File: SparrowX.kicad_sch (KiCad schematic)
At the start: 25 parts, among them J1 NORTH, J2 SOUTH, J3 WEST, J4 EAST, U1 TPS629210-Q1, U2 LD49100PU33RY, U3 STM32G0B1CBU6, U4 TCAN332G, U5 TCAN332G

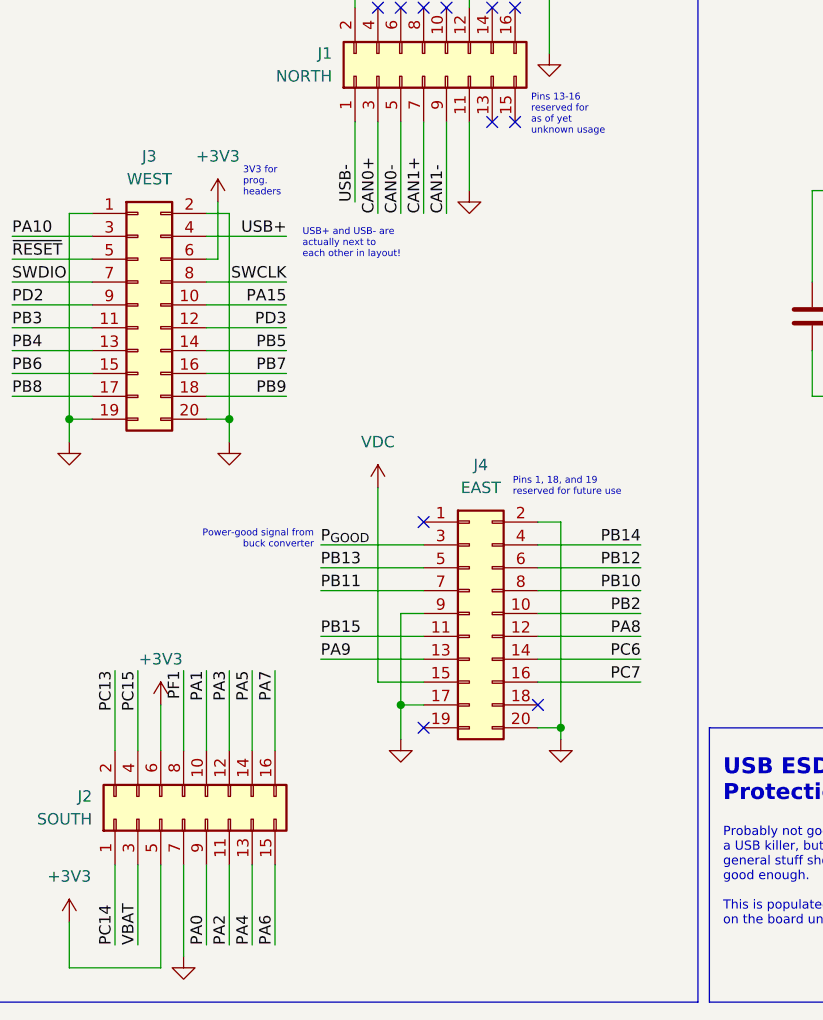
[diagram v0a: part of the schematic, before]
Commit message: Oops: fix missing PF0 pin
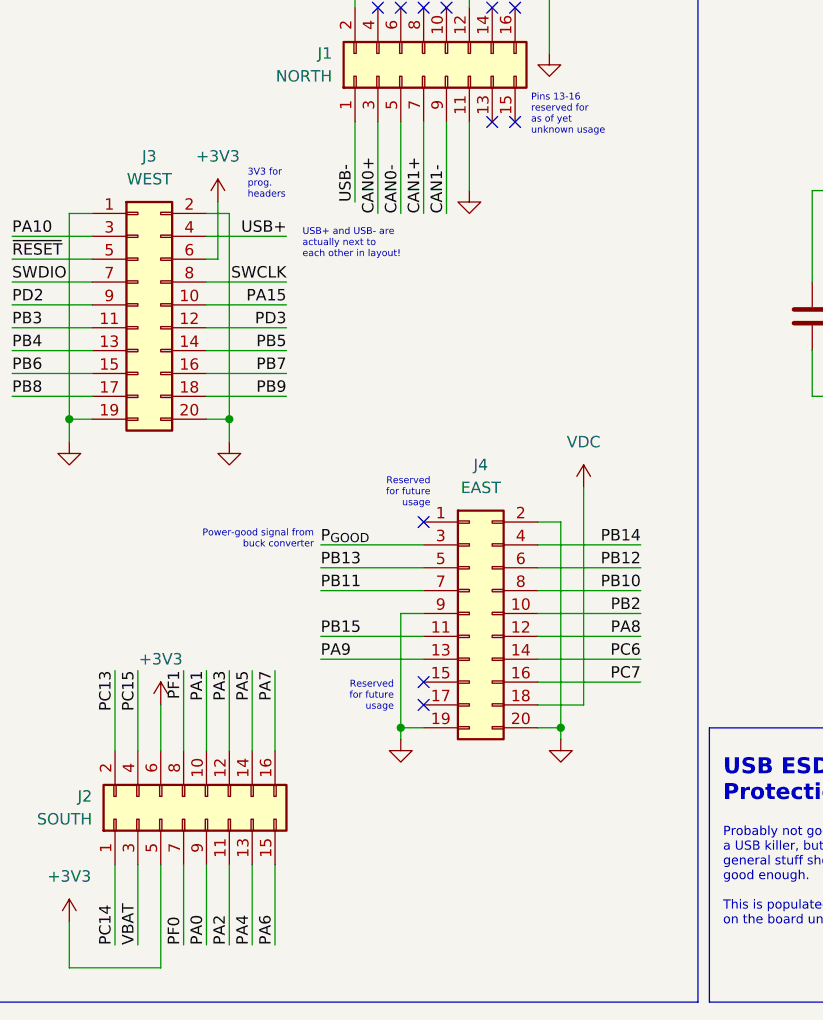
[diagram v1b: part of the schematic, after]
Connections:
- net GND: now also J4.19 (Pin_19); no longer J2.7 (Pin_7), J4.17 (Pin_17)
- net PF0: now also J2.7 (Pin_7)
- net VDC: now also J4.18 (Pin_18); no longer J4.15 (Pin_15)
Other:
- note added: "Reserved for future usage"
- note removed: "Pins 1, 18, and 19 reserved for future use"
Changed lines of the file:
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@@
 	)
 	(junction
-		(at 64.77 162.56)
-		(diameter 0)
-		(color 0 0 0 0)
-	)
-	(junction
 		(at 83.82 57.15)
 		(diameter 0)
@@
 	)
 	(junction
+		(at 64.77 165.1)
+		(diameter 0)
+		(color 0 0 0 0)
+	)
+	(junction
 		(at 30.48 33.02)
 		(diameter 0)
@@
 	)
 	(no_connect
-		(at 67.31 165.1)
-	)
-	(no_connect
-		(at 80.01 162.56)
+		(at 67.31 162.56)
 	)
 	(no_connect
@@
 	)
 	(no_connect
+		(at 67.31 160.02)
+	)
+	(no_connect
 		(at 67.31 142.24)
 	)
@@
 	(wire
 		(pts
+			(xy 85.09 138.43) (xy 85.09 162.56)
+		)
+		(stroke
+			(width 0)
+			(type default)
+		)
+	)
+	(wire
+		(pts
 			(xy 114.3 76.2) (xy 123.19 76.2)
 		)
@@
 	(wire
 		(pts
+			(xy 85.09 162.56) (xy 80.01 162.56)
+		)
+		(stroke
+			(width 0)
+			(type default)
+		)
+	)
+	(wire
+		(pts
 			(xy 119.38 33.02) (xy 123.19 33.02)
 		)
@@
 	(wire
 		(pts
-			(xy 40.64 180.34) (xy 40.64 190.5)
-		)
-		(stroke
-			(width 0)
-			(type default)
-		)
-	)
-	(wire
-		(pts
 			(xy 35.56 167.64) (xy 35.56 158.75)
 		)
@@
 	(wire
 		(pts
-			(xy 64.77 166.37) (xy 64.77 162.56)
+			(xy 64.77 166.37) (xy 64.77 165.1)
 		)
 		(stroke
@@
 	(wire
 		(pts
-			(xy 62.23 160.02) (xy 67.31 160.02)
-		)
-		(stroke
-			(width 0)
-			(type default)
-		)
-	)
-	(wire
-		(pts
 			(xy 64.77 45.72) (xy 66.04 45.72)
 		)
@@
 	(wire
 		(pts
+			(xy 40.64 180.34) (xy 40.64 189.23)
+		)
+		(stroke
+			(width 0)
+			(type default)
+		)
+	)
+	(wire
+		(pts
 			(xy 176.53 82.55) (xy 200.66 82.55)
 		)
@@
 	(wire
 		(pts
-			(xy 64.77 162.56) (xy 64.77 152.4)
+			(xy 64.77 152.4) (xy 64.77 165.1)
 		)
 		(stroke
@@
 	(wire
 		(pts
-			(xy 62.23 138.43) (xy 62.23 160.02)
-		)
-		(stroke
-			(width 0)
-			(type default)
-		)
-	)
-	(wire
-		(pts
-			(xy 64.77 162.56) (xy 67.31 162.56)
+			(xy 64.77 165.1) (xy 67.31 165.1)
 		)
 		(stroke
@@
 		)
 	)
+	(text "Reserved\nfor future\nusage"
+		(exclude_from_sim no)
+		(at 64.008 163.322 0)
+		(effects
+			(font
+				(size 0.762 0.762)
+			)
+			(justify right bottom)
+		)
+	)
 	(text "Idea: have enough pins to break\neverything out, yet still be relatively \neasy to hand solder the connectors and\nmake low-cost carrier boards for"
 		(exclude_from_sim no)
@@
 	(text "3V3 for\nprog.\nheaders"
 		(exclude_from_sim no)
-		(at 47.244 106.172 0)
+		(at 47.752 106.426 0)
 		(effects
 			(font
@@
 		)
 	)
-	(text "Pins 1, 18, and 19\nreserved for future use"
+	(text "Reserved\nfor future\nusage"
 		(exclude_from_sim no)
-		(at 77.216 139.446 0)
+		(at 68.072 140.716 0)
 		(effects
 			(font
 				(size 0.762 0.762)
 			)
-			(justify left bottom)
+			(justify right bottom)
 		)
 	)
@@
 		)
 	)
+	(label "PF0"
+		(at 40.64 189.23 90)
+		(fields_autoplaced yes)
+		(effects
+			(font
+				(size 1.27 1.27)
+			)
+			(justify left bottom)
+		)
+	)
 	(label "CAN0+"
 		(at 278.13 69.85 180)
@@
 	(symbol
 		(lib_id "power:VDC")
-		(at 62.23 138.43 0)
+		(at 85.09 138.43 0)
 		(unit 1)
 		(exclude_from_sim no)
@@
 		(dnp no)
 		(property "Reference" "#PWR017"
-			(at 62.23 140.97 0)
+			(at 85.09 140.97 0)
 			(effects
 				(font
@@
 		)
 		(property "Value" "VDC"
-			(at 62.23 133.35 0)
+			(at 85.09 133.35 0)
 			(effects
 				(font
@@
 		)
 		(property "Footprint" ""
-			(at 62.23 138.43 0)
+			(at 85.09 138.43 0)
 			(effects
 				(font
@@
 		)
 		(property "Datasheet" ""
-			(at 62.23 138.43 0)
+			(at 85.09 138.43 0)
 			(effects
 				(font
@@
 		)
 		(property "Description" ""
-			(at 62.23 138.43 0)
+			(at 85.09 138.43 0)
 			(effects
 				(font
@@
 					(unit 1)
 				)
-			)
-		)
-	)
-	(symbol
-		(lib_name "GND_1")
-		(lib_id "power:GND")
-		(at 40.64 190.5 0)
-		(unit 1)
-		(exclude_from_sim no)
-		(in_bom yes)
-		(on_board yes)
-		(dnp no)
-		(fields_autoplaced yes)
-		(property "Reference" "#PWR022"
-			(at 40.64 196.85 0)
-			(effects
-				(font
-					(size 1.27 1.27)
-				)
-				(hide yes)
-			)
-		)
-		(property "Value" "GND"
-			(at 40.64 195.58 0)
-			(effects
-				(font
-					(size 1.27 1.27)
-				)
-				(hide yes)
-			)
-		)
-		(property "Footprint" ""
-			(at 40.64 190.5 0)
-			(effects
-				(font
-					(size 1.27 1.27)
-				)
-				(hide yes)
-			)
-		)
-		(property "Datasheet" ""
-			(at 40.64 190.5 0)
-			(effects
-				(font
-					(size 1.27 1.27)
-				)
-				(hide yes)
-			)
-		)
-		(property "Description" "Power symbol creates a global label with name \"GND\" , ground"
-			(at 40.64 190.5 0)
-			(effects
-				(font
-					(size 1.27 1.27)
-				)
-				(hide yes)
-			)
-		)
-		(pin "1"
-		)
-		(instances
-			(project "SparrowX"
-				(path "/c35a64e4-2c93-4785-901b-32ffcab28aed"
-					(reference "#PWR022")
-					(unit 1)
-				)

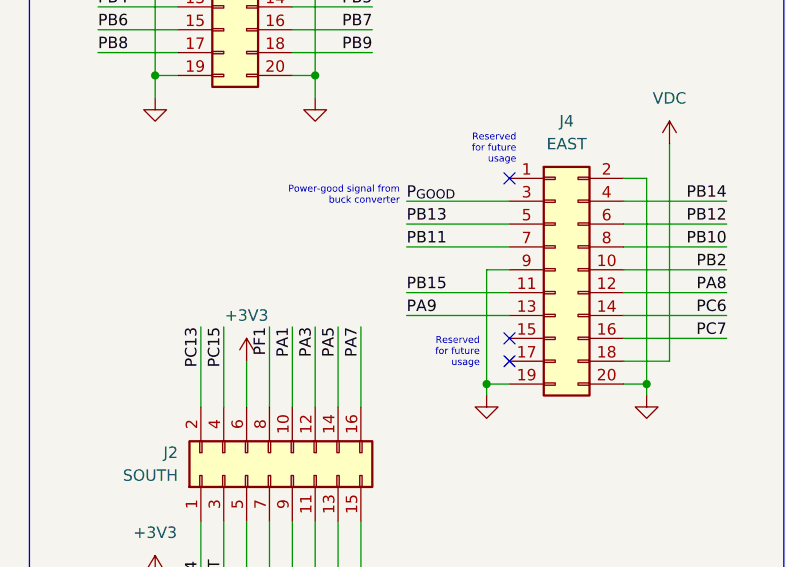
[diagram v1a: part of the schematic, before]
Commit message: Move power good signal pin for better layout
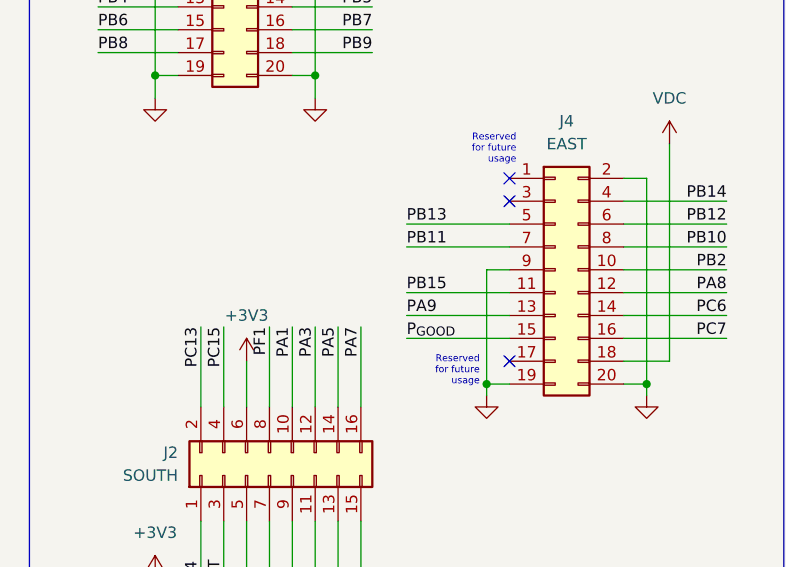
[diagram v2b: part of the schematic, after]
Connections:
- net P_{GOOD}: now also J4.15 (Pin_15); no longer J4.3 (Pin_3)
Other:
- note removed: "Power-good signal from buck converter"
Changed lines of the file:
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@@
 	)
 	(no_connect
-		(at 67.31 160.02)
+		(at 67.31 144.78)
 	)
 	(no_connect
@@
 	(wire
 		(pts
-			(xy 55.88 144.78) (xy 67.31 144.78)
+			(xy 55.88 160.02) (xy 67.31 160.02)
 		)
 		(stroke
@@
 	(text "Reserved\nfor future\nusage"
 		(exclude_from_sim no)
-		(at 64.008 163.322 0)
+		(at 64.008 165.354 0)
 		(effects
 			(font
@@
 		)
 	)
-	(text "Power-good signal from\nbuck converter"
-		(exclude_from_sim no)
-		(at 55.118 145.288 0)
-		(effects
-			(font
-				(size 0.762 0.762)
-			)
-			(justify right bottom)
-		)
-	)
 	(text "USB ESD\nProtection"
 		(exclude_from_sim no)
@@
 	)
 	(label "P_{GOOD}"
-		(at 55.88 144.78 0)
+		(at 55.88 160.02 0)
 		(fields_autoplaced yes)
 		(effects

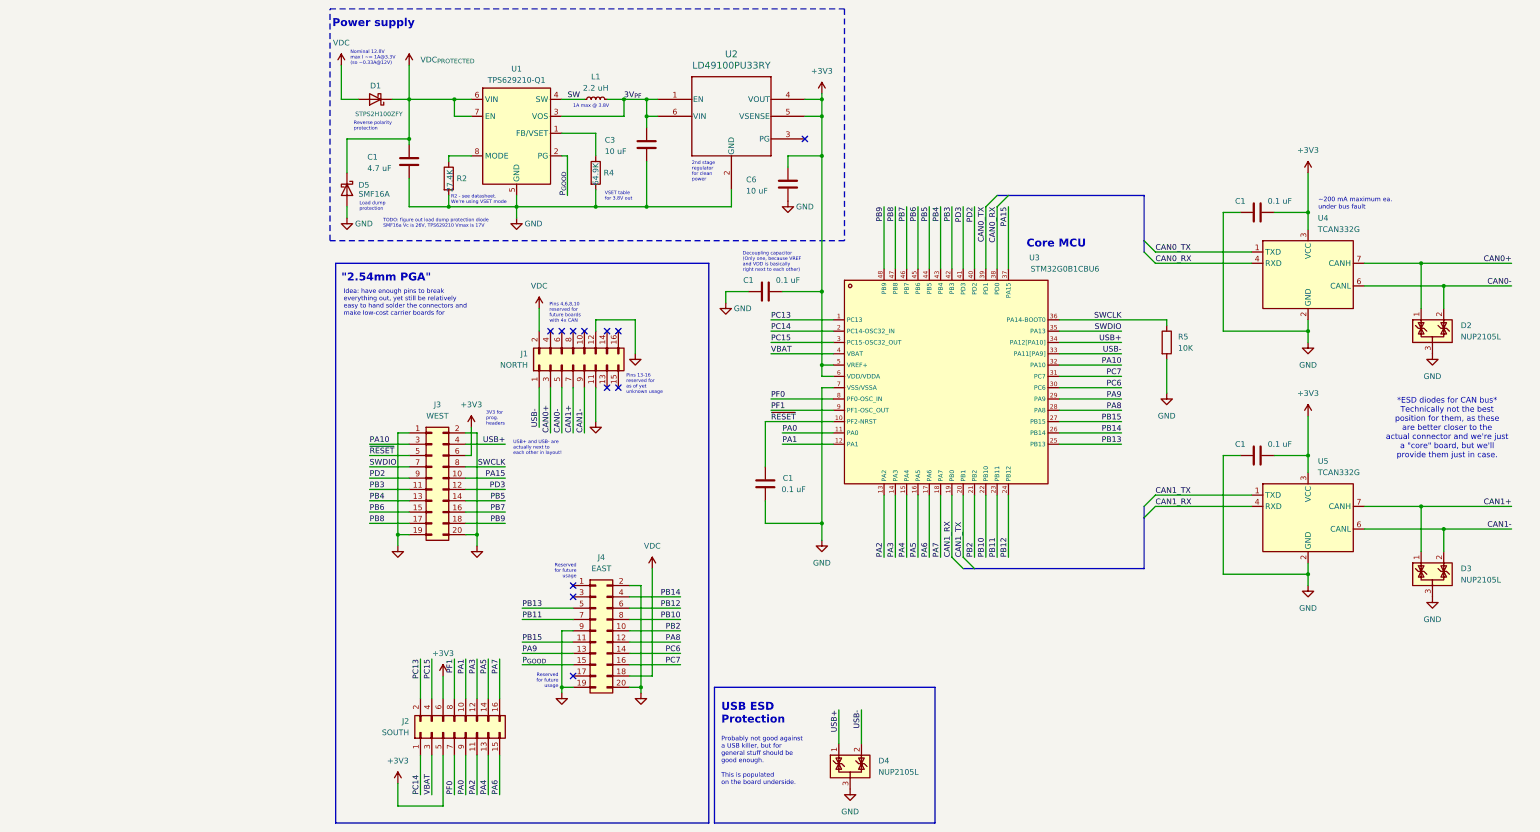
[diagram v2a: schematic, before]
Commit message: Add VREF+ RC-filter; silkscreen adjustments
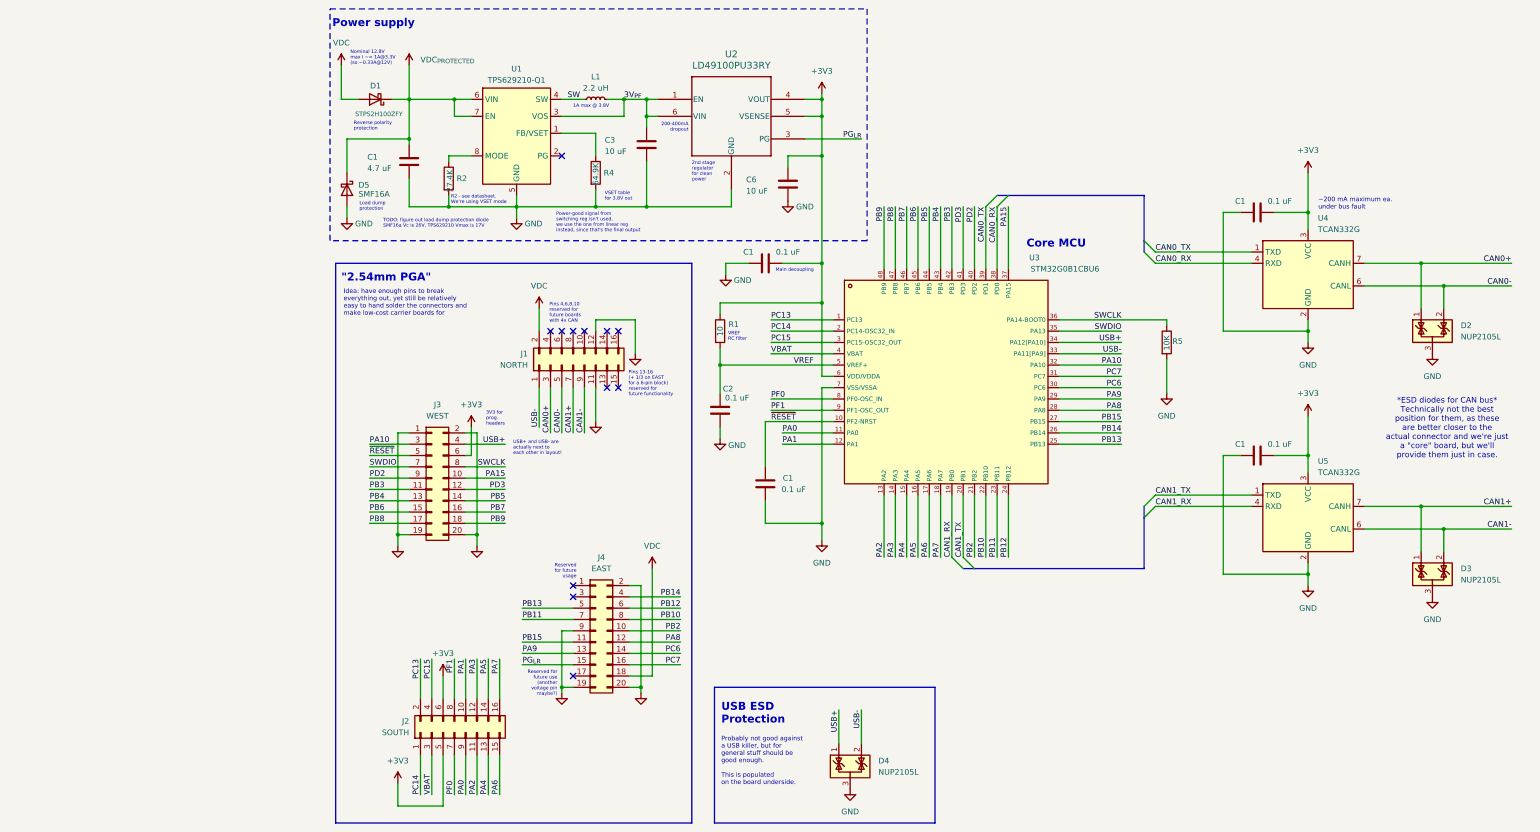
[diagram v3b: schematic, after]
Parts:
- added C2: 0.1 uF, Capacitor_SMD:C_0201_0603Metric, symbol Device:C
- added R1: 10, Resistor_SMD:R_0201_0603Metric, symbol Device:R
- C1: footprint Capacitor_SMD:C_0402_1005Metric -> Capacitor_SMD:C_0201_0603Metric
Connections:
- net +3V3: now also R1.1; no longer U3.5 (VREF+)
- net GND: now also C2.2
- net PG_{LR}: now reaches U2.3 (PG)
- net PG_{LR}: now also J4.15 (Pin_15)
- net P_{GOOD}: no longer names the net of U1.2 (PG)
- net P_{GOOD}: no longer J4.15 (Pin_15)
- new net VREF: C2.1, R1.2, U3.5 (VREF+)
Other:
- note added: "200-400mA dropout"
- note added: "Main decoupling"
- note added: "Pins 13-16 (+ 1/3 on EAST for a 6-pin block) reserved for future functionality"
- note added: "Power-good signal from switching reg isn't used, we use the one from linear reg instead, since that's the final output"
- note added: "Reserved for future use (another voltage pin maybe?)"
- note added: "VREF RC filter"
- note removed: "Decoupling capacitor (Only one, because VREF and VDD is basically right next to each other)"
- note removed: "Pins 13-16 reserved for as of yet unknown usage"
- moved on the sheet: C1

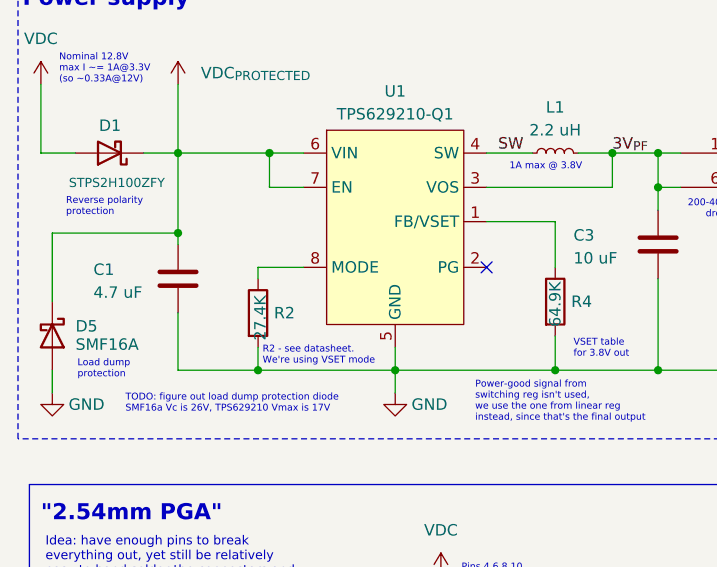
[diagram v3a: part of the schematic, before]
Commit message: Tie power good pin of TPS629210 to GND (see datasheet section 8.3.5)
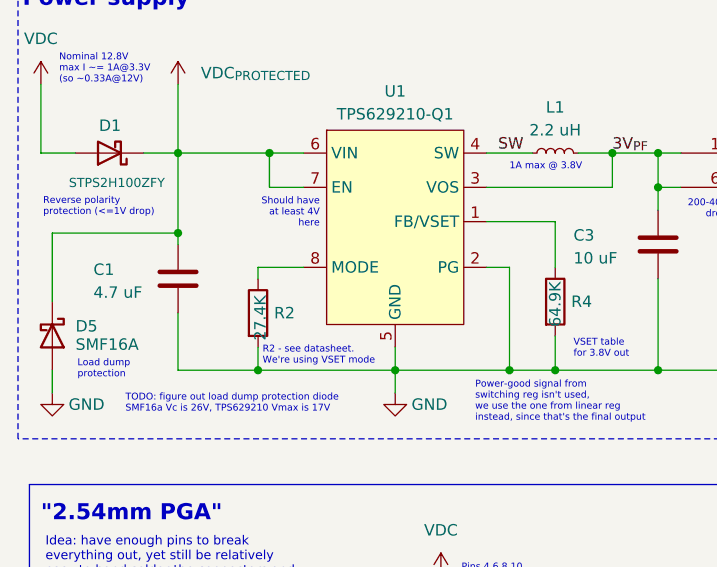
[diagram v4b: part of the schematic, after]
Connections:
- net GND: now also U1.2 (PG)
- no-connect marks 12 -> 11
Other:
- note added: "Reverse polarity protection (<=1V drop)"
- note added: "Should have at least 4V here"
- note removed: "Reverse polarity protection"
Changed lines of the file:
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@@
+	)
+	(junction
+		(at 67.31 57.15)
+		(diameter 0)
+		(color 0 0 0 0)
 	)
 	(junction
@@
 	)
 	(no_connect
-		(at 64.77 45.72)
-	)
-	(no_connect
 		(at 64.77 85.09)
 	)
@@
 	(wire
 		(pts
+			(xy 67.31 57.15) (xy 72.39 57.15)
+		)
+		(stroke
+			(width 0)
+			(type default)
+		)
+	)
+	(wire
+		(pts
 			(xy 30.48 118.11) (xy 21.59 118.11)
 		)
@@
 	(wire
 		(pts
-			(xy 54.61 57.15) (xy 72.39 57.15)
+			(xy 54.61 57.15) (xy 67.31 57.15)
 		)
 		(stroke
@@
 	(wire
 		(pts
+			(xy 64.77 45.72) (xy 67.31 45.72)
+		)
+		(stroke
+			(width 0)
+			(type default)
+		)
+	)
+	(wire
+		(pts
 			(xy 43.18 123.19) (xy 52.07 123.19)
 		)
@@
 		(pts
 			(xy 213.36 58.42) (xy 213.36 85.09)
+		)
+		(stroke
+			(width 0)
+			(type default)
+		)
+	)
+	(wire
+		(pts
+			(xy 67.31 45.72) (xy 67.31 57.15)
 		)
 		(stroke
@@
 		)
 	)
+	(text "Should have\nat least 4V\nhere"
+		(exclude_from_sim no)
+		(at 46.228 41.402 0)
+		(effects
+			(font
+				(size 0.762 0.762)
+			)
+			(justify right bottom)
+		)
+	)
 	(text "USB ESD\nProtection"
 		(exclude_from_sim no)
@@
 		)
 	)
-	(text "Reverse polarity\nprotection"
+	(text "Reverse polarity\nprotection (<=1V drop)"
 		(exclude_from_sim no)
-		(at 18.034 40.132 0)
+		(at 15.494 40.132 0)
 		(effects
 			(font
